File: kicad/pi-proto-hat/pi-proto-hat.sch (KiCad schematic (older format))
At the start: 5 parts, among them P1 Conn_02x20_Odd_Even

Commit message: R1: one GPIO connector, one I2C connector
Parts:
- added J1: Conn_01x24_Male, Connector_PinHeader_2.54mm:PinHeader_1x24_P2.54mm_Vertical, symbol Connector:Conn_01x24_Male
- added J2: Conn_I2C, Connector_PinHeader_2.54mm:PinHeader_1x04_P2.54mm_Vertical, symbol Connector:Conn_01x04_Male
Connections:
- net +3V3: now also J2.4 (Pin_4)
- net GND: now also J2.3 (Pin_3)
- net GPIO10(SPI0_MOSI): now also J1.14 (Pin_14)
- net GPIO11(SPI0_SCK): now also J1.12 (Pin_12)
- net GPIO12(PWM0): now also J1.7 (Pin_7)
- net GPIO13(PWM1): now also J1.6 (Pin_6)
- net GPIO14(TXD0): now also J1.24 (Pin_24)
- net GPIO15(RXD0): now also J1.23 (Pin_23)
- net GPIO16: now also J1.5 (Pin_5)
- net GPIO17(GEN0): now also J1.21 (Pin_21)
- net GPIO18(GEN1)(PWM0): now also J1.20 (Pin_20)
- net GPIO19(SPI1_MISO): now also J1.4 (Pin_4)
- net GPIO2(SDA1): now also J2.2 (Pin_2)
- net GPIO20(SPI1_MOSI): now also J1.3 (Pin_3)
- net GPIO21(SPI1_SCK): now also J1.2 (Pin_2)
- net GPIO22(GEN3): now also J1.18 (Pin_18)
- net GPIO23(GEN4): now also J1.17 (Pin_17)
- net GPIO24(GEN5): now also J1.16 (Pin_16)
- net GPIO25(GEN6): now also J1.15 (Pin_15)
- net GPIO26: now also J1.1 (Pin_1)
- net GPIO27(GEN2): now also J1.19 (Pin_19)
- net GPIO3(SCL1): now also J2.1 (Pin_1)
- net GPIO4(GCLK): now also J1.22 (Pin_22)
- net GPIO5: now also J1.9 (Pin_9)
- net GPIO6: now also J1.8 (Pin_8)
- net GPIO9(SPI0_MISO): now also J1.13 (Pin_13)
- net GPIO7(SPI1_CE_N) renamed GPIO7(SPI1_CE_1)
- net GPIO7(SPI1_CE_1): now also J1.10 (Pin_10)
- net GPIO8(SPI0_CE_N) renamed GPIO8(SPI0_CE_0)
- net GPIO8(SPI0_CE_0): now also J1.11 (Pin_11)
- net ID_SC: no longer names the net of P1.28 (Pin_28)
- net ID_SD: no longer names the net of P1.27 (Pin_27)
- no-connect marks 0 -> 2
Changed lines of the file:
@@
 	1250 2200 2400 2200
 Wire Wire Line
-	2400 2400 1250 2400
-Wire Wire Line
 	1250 2500 2400 2500
 Wire Wire Line
@@
 Wire Wire Line
 	2900 2300 3950 2300
-Wire Wire Line
-	2900 2400 3950 2400
 Wire Wire Line
 	2900 2100 3950 2100
@@
 Text Label 1250 2200 0    50   ~ 0
 GPIO11(SPI0_SCK)
-Text Label 1250 2400 0    50   ~ 0
-ID_SD
 Text Label 1250 2500 0    50   ~ 0
 GPIO5
@@
 Text Label 3950 2600 2    50   ~ 0
 GPIO12(PWM0)
-Text Label 3950 2400 2    50   ~ 0
-ID_SC
 Text Label 3950 2300 2    50   ~ 0
-GPIO7(SPI1_CE_N)
+GPIO7(SPI1_CE_1)
 Text Label 3950 2200 2    50   ~ 0
-GPIO8(SPI0_CE_N)
+GPIO8(SPI0_CE_0)
 Text Label 3950 2100 2    50   ~ 0
 GPIO25(GEN6)
@@
 	3000 1700 3000 2000
 $Comp
-L power:GND #PWR?
+L power:GND #PWR0101
 U 1 1 5E32FD4E
 P 800 1050
-F 0 "#PWR?" H 800 800 50  0001 C CNN
+F 0 "#PWR0101" H 800 800 50  0001 C CNN
 F 1 "GND" H 805 877 50  0000 C CNN
 F 2 "" H 800 1050 50  0001 C CNN
@@
 $EndComp
 $Comp
-L power:+3.3V #PWR?
+L power:+3.3V #PWR0102
 U 1 1 5E330101
 P 800 1700
-F 0 "#PWR?" H 800 1550 50  0001 C CNN
+F 0 "#PWR0102" H 800 1550 50  0001 C CNN
 F 1 "+3.3V" H 815 1873 50  0000 C CNN
 F 2 "" H 800 1700 50  0001 C CNN
@@
 $EndComp
 $Comp
-L power:+5V #PWR?
+L power:+5V #PWR0103
 U 1 1 5E33350C
 P 800 2450
-F 0 "#PWR?" H 800 2300 50  0001 C CNN
+F 0 "#PWR0103" H 800 2300 50  0001 C CNN
 F 1 "+5V" H 815 2623 50  0000 C CNN
 F 2 "" H 800 2450 50  0001 C CNN
@@
 $EndComp
 $Comp
-L power:PWR_FLAG #FLG?
+L power:PWR_FLAG #FLG0101
 U 1 1 5E335D20
 P 800 1500
-F 0 "#FLG?" H 800 1575 50  0001 C CNN
+F 0 "#FLG0101" H 800 1575 50  0001 C CNN
 F 1 "PWR_FLAG" H 800 1673 50  0000 C CNN
 F 2 "" H 800 1500 50  0001 C CNN
@@
 $EndComp
 $Comp
-L power:PWR_FLAG #FLG?
+L power:PWR_FLAG #FLG0102
 U 1 1 5E3368A3
 P 800 2200
-F 0 "#FLG?" H 800 2275 50  0001 C CNN
+F 0 "#FLG0102" H 800 2275 50  0001 C CNN
 F 1 "PWR_FLAG" H 800 2373 50  0000 C CNN
 F 2 "" H 800 2200 50  0001 C CNN
@@
 $EndComp
 $Comp
-L power:PWR_FLAG #FLG?
+L power:PWR_FLAG #FLG0103
 U 1 1 5E337128
 P 800 800
-F 0 "#FLG?" H 800 875 50  0001 C CNN
+F 0 "#FLG0103" H 800 875 50  0001 C CNN
 F 1 "PWR_FLAG" H 800 973 50  0000 C CNN
 F 2 "" H 800 800 50  0001 C CNN
@@
 Wire Wire Line
 	800  2200 800  2450
+$Comp
+L Connector:Conn_01x24_Male J1
+U 1 1 5E33021D
+P 5500 2150
+F 0 "J1" H 5900 700 50  0000 R CNN
+F 1 "Conn_01x24_Male" H 6100 800 50  0000 R CNN
+F 2 "Connector_PinHeader_2.54mm:PinHeader_1x24_P2.54mm_Vertical" H 5500 2150 50  0001 C CNN
+F 3 "~" H 5500 2150 50  0001 C CNN
+	1    5500 2150
+	-1   0    0    1
+$EndComp
+Text Label 4900 950  2    50   ~ 0
+GPIO14(TXD0)
+Text Label 4900 1050 2    50   ~ 0
+GPIO15(RXD0)
+Text Label 4900 1150 2    50   ~ 0
+GPIO4(GCLK)
+Text Label 4900 1250 2    50   ~ 0
+GPIO17(GEN0)
+Text Label 4900 1350 2    50   ~ 0
+GPIO18(GEN1)(PWM0)
+Text Label 4900 1450 2    50   ~ 0
+GPIO27(GEN2)
+Text Label 4900 1550 2    50   ~ 0
+GPIO22(GEN3)
+Text Label 4900 1650 2    50   ~ 0
+GPIO23(GEN4)
+Text Label 4900 1850 2    50   ~ 0
+GPIO25(GEN6)
+Text Label 4900 1950 2    50   ~ 0
+GPIO10(SPI0_MOSI)
+Text Label 4900 2050 2    50   ~ 0
+GPIO9(SPI0_MISO)
+Text Label 4900 2150 2    50   ~ 0
+GPIO11(SPI0_SCK)
+Text Label 4900 2250 2    50   ~ 0
+GPIO8(SPI0_CE_0)
+Text Label 4900 2350 2    50   ~ 0
+GPIO7(SPI1_CE_1)
+Text Label 4900 2450 2    50   ~ 0
+GPIO5
+Text Label 4900 2550 2    50   ~ 0
+GPIO6
+Text Label 4900 2650 2    50   ~ 0
+GPIO12(PWM0)
+Text Label 4900 2750 2    50   ~ 0
+GPIO13(PWM1)
+Text Label 4900 2850 2    50   ~ 0
+GPIO16
+Text Label 4900 2950 2    50   ~ 0
+GPIO19(SPI1_MISO)
+Text Label 4900 3050 2    50   ~ 0
+GPIO20(SPI1_MOSI)
+Text Label 4900 3150 2    50   ~ 0
+GPIO21(SPI1_SCK)
+Text Label 4900 3250 2    50   ~ 0
+GPIO26
+Wire Wire Line
+	4900 950  5300 950
+Wire Wire Line
+	4900 1050 5300 1050
+Wire Wire Line
+	4900 1150 5300 1150
+Wire Wire Line
+	4900 1250 5300 1250
+Wire Wire Line
+	4900 1350 5300 1350
+Wire Wire Line
+	4900 1450 5300 1450
+Wire Wire Line
+	4900 1550 5300 1550
+Wire Wire Line
+	4900 1650 5300 1650
+Wire Wire Line
+	4900 1750 5300 1750
+Wire Wire Line
+	4900 1850 5300 1850
+Wire Wire Line
+	4900 1950 5300 1950
+Wire Wire Line
+	4900 2050 5300 2050
+Wire Wire Line
+	4900 2150 5300 2150
+Wire Wire Line
+	4900 2250 5300 2250
+Wire Wire Line
+	4900 2350 5300 2350
+Wire Wire Line
+	4900 2450 5300 2450
+Wire Wire Line
+	4900 2550 5300 2550
+Wire Wire Line
+	4900 2650 5300 2650
+Wire Wire Line
+	4900 2750 5300 2750
+Wire Wire Line
+	4900 2850 5300 2850
+Wire Wire Line
+	4900 2950 5300 2950
+Wire Wire Line
+	4900 3050 5300 3050
+Wire Wire Line
+	4900 3150 5300 3150
+Wire Wire Line
+	4900 3250 5300 3250
+Text Label 4900 1750 2    50   ~ 0
+GPIO24(GEN5)
+NoConn ~ 2400 2400
+NoConn ~ 2900 2400
+$Comp
+L Connector:Conn_01x04_Male J2
+U 1 1 5E3AE486
+P 6400 1150
+F 0 "J2" H 6550 700 50  0000 R CNN
+F 1 "Conn_I2C" H 6650 800 50  0000 R CNN
+F 2 "Connector_PinHeader_2.54mm:PinHeader_1x04_P2.54mm_Vertical" H 6400 1150 50  0001 C CNN
+F 3 "~" H 6400 1150 50  0001 C CNN
+	1    6400 1150
+	-1   0    0    1
+$EndComp
+$Comp
+L power:+3.3V #PWR0104
+U 1 1 5E3B69CB
+P 6050 950
+F 0 "#PWR0104" H 6050 800 50  0001 C CNN
+F 1 "+3.3V" V 6050 1200 50  0000 C CNN
+F 2 "" H 6050 950 50  0000 C CNN
+F 3 "" H 6050 950 50  0000 C CNN
+	1    6050 950
+	0    -1   -1   0
+$EndComp
+$Comp
+L power:GND #PWR0105
+U 1 1 5E3BF524
+P 6050 1050
+F 0 "#PWR0105" H 6050 800 50  0001 C CNN
+F 1 "GND" H 6050 900 50  0000 C CNN
+F 2 "" H 6050 1050 50  0000 C CNN
+F 3 "" H 6050 1050 50  0000 C CNN
+	1    6050 1050
+	0    1    1    0
+$EndComp
+Text Label 6050 1250 2    50   ~ 0
+GPIO3(SCL1)
+Text Label 6050 1150 2    50   ~ 0
+GPIO2(SDA1)
+Wire Wire Line
+	6050 950  6200 950
+Wire Wire Line
+	6050 1050 6200 1050
+Wire Wire Line
+	6050 1150 6200 1150
+Wire Wire Line
+	6050 1250 6200 1250
 $EndSCHEMATC

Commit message: R2: 1xUART+GND, 2xI2C+VCC+GND
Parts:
- added I2C2: Conn_I2C, Connector_PinHeader_2.54mm:PinHeader_1x04_P2.54mm_Vertical, symbol Connector:Conn_01x04_Male
- added UART1: Conn_01x03_Male, Connector_PinHeader_2.54mm:PinHeader_1x03_P2.54mm_Vertical, symbol Connector:Conn_01x03_Male
- J1: value Conn_01x24_Male -> Conn_01x22_Male; footprint Connector_PinHeader_2.54mm:PinHeader_1x24_P2.54mm_Vertical -> Connector_PinHeader_2.54mm:PinHeader_1x22_P2.54mm_Vertical; symbol Connector:Conn_01x24_Male -> Connector:Conn_01x22_Male
- renumbered J2 to I2C1
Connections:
- net +3V3: now also I2C2.4 (Pin_4)
- net GND: now also I2C2.3 (Pin_3), UART1.1 (Pin_1)
- net GPIO14(TXD0): now also UART1.3 (Pin_3); no longer J1.24 (Pin_24)
- net GPIO15(RXD0): now also UART1.2 (Pin_2); no longer J1.23 (Pin_23)
- net GPIO17(GEN0): now also J1.20 (Pin_20); no longer J1.21 (Pin_21)
- net GPIO18(GEN1)(PWM0): now also J1.21 (Pin_21); no longer J1.20 (Pin_20)
- net GPIO2(SDA1): now also I2C1.1 (Pin_1), I2C2.1 (Pin_1); no longer I2C1.2 (Pin_2)
- net GPIO22(GEN3): now also J1.17 (Pin_17); no longer J1.18 (Pin_18)
- net GPIO23(GEN4): now also J1.18 (Pin_18); no longer J1.17 (Pin_17)
- net GPIO3(SCL1): now also I2C1.2 (Pin_2), I2C2.2 (Pin_2); no longer I2C1.1 (Pin_1)
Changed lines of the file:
@@
 Sheet 1 1
 Title "Pi-Proto-Hat"
-Date "2020-01-30"
-Rev "1"
+Date "2020-02-15"
+Rev "2"
 Comp "Bernhard Bablok"
 Comment1 "https://github.com/bablokb/pi-proto-hat"
@@
 	800  2200 800  2450
 $Comp
-L Connector:Conn_01x24_Male J1
+L Connector:Conn_01x22_Male J1
 U 1 1 5E33021D
-P 5500 2150
+P 5500 2050
 F 0 "J1" H 5900 700 50  0000 R CNN
-F 1 "Conn_01x24_Male" H 6100 800 50  0000 R CNN
-F 2 "Connector_PinHeader_2.54mm:PinHeader_1x24_P2.54mm_Vertical" H 5500 2150 50  0001 C CNN
-F 3 "~" H 5500 2150 50  0001 C CNN
-	1    5500 2150
+F 1 "Conn_01x22_Male" H 6150 800 50  0000 R CNN
+F 2 "Connector_PinHeader_2.54mm:PinHeader_1x22_P2.54mm_Vertical" H 5500 2050 50  0001 C CNN
+F 3 "~" H 5500 2050 50  0001 C CNN
+	1    5500 2050
 	-1   0    0    1
 $EndComp
 Text Label 4900 950  2    50   ~ 0
-GPIO14(TXD0)
+GPIO4(GCLK)
+Text Label 4900 1150 2    50   ~ 0
+GPIO17(GEN0)
 Text Label 4900 1050 2    50   ~ 0
-GPIO15(RXD0)
-Text Label 4900 1150 2    50   ~ 0
-GPIO4(GCLK)
+GPIO18(GEN1)(PWM0)
 Text Label 4900 1250 2    50   ~ 0
-GPIO17(GEN0)
-Text Label 4900 1350 2    50   ~ 0
-GPIO18(GEN1)(PWM0)
+GPIO27(GEN2)
 Text Label 4900 1450 2    50   ~ 0
-GPIO27(GEN2)
-Text Label 4900 1550 2    50   ~ 0
 GPIO22(GEN3)
 Text Label 4900 1650 2    50   ~ 0
-GPIO23(GEN4)
+GPIO25(GEN6)
+Text Label 4900 1750 2    50   ~ 0
+GPIO10(SPI0_MOSI)
 Text Label 4900 1850 2    50   ~ 0
-GPIO25(GEN6)
+GPIO9(SPI0_MISO)
 Text Label 4900 1950 2    50   ~ 0
-GPIO10(SPI0_MOSI)
+GPIO11(SPI0_SCK)
 Text Label 4900 2050 2    50   ~ 0
-GPIO9(SPI0_MISO)
+GPIO8(SPI0_CE_0)
 Text Label 4900 2150 2    50   ~ 0
-GPIO11(SPI0_SCK)
+GPIO7(SPI1_CE_1)
 Text Label 4900 2250 2    50   ~ 0
-GPIO8(SPI0_CE_0)
+GPIO5
 Text Label 4900 2350 2    50   ~ 0
-GPIO7(SPI1_CE_1)
+GPIO6
 Text Label 4900 2450 2    50   ~ 0
-GPIO5
+GPIO12(PWM0)
 Text Label 4900 2550 2    50   ~ 0
-GPIO6
+GPIO13(PWM1)
 Text Label 4900 2650 2    50   ~ 0
-GPIO12(PWM0)
+GPIO16
 Text Label 4900 2750 2    50   ~ 0
-GPIO13(PWM1)
+GPIO19(SPI1_MISO)
 Text Label 4900 2850 2    50   ~ 0
-GPIO16
+GPIO20(SPI1_MOSI)
 Text Label 4900 2950 2    50   ~ 0
-GPIO19(SPI1_MISO)
+GPIO21(SPI1_SCK)
 Text Label 4900 3050 2    50   ~ 0
-GPIO20(SPI1_MOSI)
-Text Label 4900 3150 2    50   ~ 0
-GPIO21(SPI1_SCK)
-Text Label 4900 3250 2    50   ~ 0
 GPIO26
 Wire Wire Line
@@
 Wire Wire Line
 	4900 3050 5300 3050
-Wire Wire Line
-	4900 3150 5300 3150
-Wire Wire Line
-	4900 3250 5300 3250
-Text Label 4900 1750 2    50   ~ 0
+Text Label 4900 1550 2    50   ~ 0
 GPIO24(GEN5)
 NoConn ~ 2400 2400
 NoConn ~ 2900 2400
 $Comp
-L Connector:Conn_01x04_Male J2
+L Connector:Conn_01x04_Male I2C1
 U 1 1 5E3AE486
 P 6400 1150
-F 0 "J2" H 6550 700 50  0000 R CNN
-F 1 "Conn_I2C" H 6650 800 50  0000 R CNN
+F 0 "I2C1" H 6750 700 50  0000 R CNN
+F 1 "Conn_I2C" H 6800 800 50  0000 R CNN
 F 2 "Connector_PinHeader_2.54mm:PinHeader_1x04_P2.54mm_Vertical" H 6400 1150 50  0001 C CNN
 F 3 "~" H 6400 1150 50  0001 C CNN
@@
 	0    1    1    0
 $EndComp
+Text Label 6050 1150 2    50   ~ 0
+GPIO3(SCL1)
 Text Label 6050 1250 2    50   ~ 0
+GPIO2(SDA1)
+Wire Wire Line
+	6050 950  6200 950
+Wire Wire Line
+	6050 1050 6200 1050
+Wire Wire Line
+	6050 1150 6200 1150
+Wire Wire Line
+	6050 1250 6200 1250
+$Comp
+L Connector:Conn_01x04_Male I2C2
+U 1 1 5E46D17D
+P 7300 1150
+F 0 "I2C2" H 7600 700 50  0000 R CNN
+F 1 "Conn_I2C" H 7650 800 50  0000 R CNN
+F 2 "Connector_PinHeader_2.54mm:PinHeader_1x04_P2.54mm_Vertical" H 7300 1150 50  0001 C CNN
+F 3 "~" H 7300 1150 50  0001 C CNN
+	1    7300 1150
+	-1   0    0    1
+$EndComp
+$Comp
+L power:+3.3V #PWR0106
+U 1 1 5E46D187
+P 6950 950
+F 0 "#PWR0106" H 6950 800 50  0001 C CNN
+F 1 "+3.3V" V 6950 1200 50  0000 C CNN
+F 2 "" H 6950 950 50  0000 C CNN
+F 3 "" H 6950 950 50  0000 C CNN
+	1    6950 950
+	0    -1   -1   0
+$EndComp
+$Comp
+L power:GND #PWR0107
+U 1 1 5E46D191
+P 6950 1050
+F 0 "#PWR0107" H 6950 800 50  0001 C CNN
+F 1 "GND" H 6950 900 50  0000 C CNN
+F 2 "" H 6950 1050 50  0000 C CNN
+F 3 "" H 6950 1050 50  0000 C CNN
+	1    6950 1050
+	0    1    1    0
+$EndComp
+Text Label 6950 1150 2    50   ~ 0
 GPIO3(SCL1)
-Text Label 6050 1150 2    50   ~ 0
+Text Label 6950 1250 2    50   ~ 0
 GPIO2(SDA1)
 Wire Wire Line
-	6050 950  6200 950
-Wire Wire Line
-	6050 1050 6200 1050
-Wire Wire Line
-	6050 1150 6200 1150
-Wire Wire Line
-	6050 1250 6200 1250
+	6950 950  7100 950
+Wire Wire Line
+	6950 1050 7100 1050
+Wire Wire Line
+	6950 1150 7100 1150
+Wire Wire Line
+	6950 1250 7100 1250
+$Comp
+L Connector:Conn_01x03_Male UART1
+U 1 1 5E470F02
+P 8100 1100
+F 0 "UART1" H 8500 700 50  0000 R CNN
+F 1 "Conn_01x03_Male" H 8600 800 50  0000 R CNN
+F 2 "Connector_PinHeader_2.54mm:PinHeader_1x03_P2.54mm_Vertical" H 8100 1100 50  0001 C CNN
+F 3 "~" H 8100 1100 50  0001 C CNN
+	1    8100 1100
+	-1   0    0    1
+$EndComp
+Text Label 7900 1000 2    50   ~ 0
+GPIO14(TXD0)
+Text Label 7900 1100 2    50   ~ 0
+GPIO15(RXD0)
+$Comp
+L power:GND #PWR0108
+U 1 1 5E4850A5
+P 7900 1200
+F 0 "#PWR0108" H 7900 950 50  0001 C CNN
+F 1 "GND" H 7900 1050 50  0000 C CNN
+F 2 "" H 7900 1200 50  0000 C CNN
+F 3 "" H 7900 1200 50  0000 C CNN
+	1    7900 1200
+	0    1    1    0
+$EndComp
+Text Label 4900 1350 2    50   ~ 0
+GPIO23(GEN4)
 $EndSCHEMATC

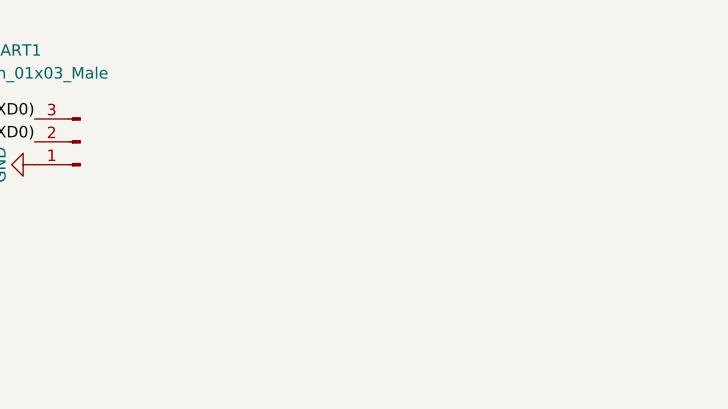
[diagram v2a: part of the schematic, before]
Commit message: R3: VCC+GND connector 22x02
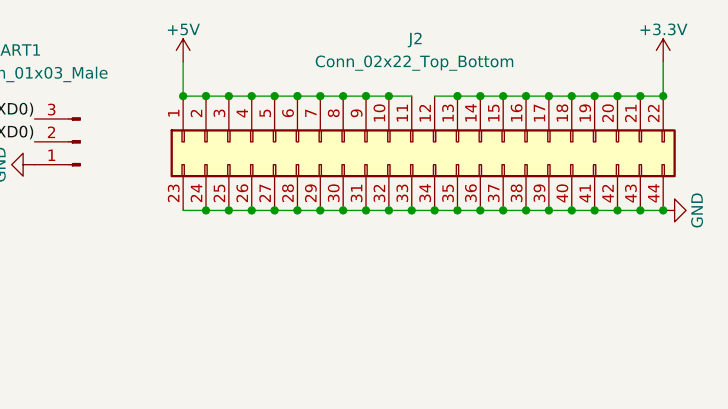
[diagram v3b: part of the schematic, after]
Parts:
- added J2: Conn_02x22_Top_Bottom, Proto_Area:Proto_Area_22x02, symbol Connector_Generic:Conn_02x22_Top_Bottom
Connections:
- net +3V3: now also J2.12 (Pin_12), J2.13 (Pin_13), J2.14 (Pin_14), J2.15 (Pin_15), J2.16 (Pin_16), J2.17 (Pin_17), J2.18 (Pin_18), J2.19 (Pin_19), J2.20 (Pin_20), J2.21 (Pin_21), J2.22 (Pin_22)
- net +5V: now also J2.1 (Pin_1), J2.10 (Pin_10), J2.11 (Pin_11), J2.2 (Pin_2), J2.3 (Pin_3), J2.4 (Pin_4), J2.5 (Pin_5), J2.6 (Pin_6), J2.7 (Pin_7), J2.8 (Pin_8), J2.9 (Pin_9)
- net GND: now also J2.23 (Pin_23), J2.24 (Pin_24), J2.25 (Pin_25), J2.26 (Pin_26), J2.27 (Pin_27), J2.28 (Pin_28), J2.29 (Pin_29), J2.30 (Pin_30), J2.31 (Pin_31), J2.32 (Pin_32), J2.33 (Pin_33), J2.34 (Pin_34), J2.35 (Pin_35), J2.36 (Pin_36), J2.37 (Pin_37), J2.38 (Pin_38), J2.39 (Pin_39), J2.40 (Pin_40), J2.41 (Pin_41), J2.42 (Pin_42), J2.43 (Pin_43), J2.44 (Pin_44)
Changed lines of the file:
@@
 Title "Pi-Proto-Hat"
 Date "2020-02-15"
-Rev "2"
+Rev "3"
 Comp "Bernhard Bablok"
 Comment1 "https://github.com/bablokb/pi-proto-hat"
@@
 	4900 2250 5300 2250
 Wire Wire Line
-	4900 2350 5300 2350
-Wire Wire Line
-	4900 2450 5300 2450
-Wire Wire Line
 	4900 2550 5300 2550
 Wire Wire Line
@@
 Wire Wire Line
 	4900 2750 5300 2750
-Wire Wire Line
-	4900 2850 5300 2850
-Wire Wire Line
-	4900 2950 5300 2950
 Wire Wire Line
 	4900 3050 5300 3050
@@
 Text Label 4900 1350 2    50   ~ 0
 GPIO23(GEN4)
+$Comp
+L Connector_Generic:Conn_02x22_Top_Bottom J2
+U 1 1 5E47EDE2
+P 9550 1100
+F 0 "J2" V 9100 1050 50  0000 L CNN
+F 1 "Conn_02x22_Top_Bottom" V 9200 650 50  0000 L CNN
+F 2 "Proto_Area:Proto_Area_22x02" H 9550 1100 50  0001 C CNN
+F 3 "~" H 9550 1100 50  0001 C CNN
+	1    9550 1100
+	0    -1   1    0
+$EndComp
+Wire Wire Line
+	4900 2350 5300 2350
+Wire Wire Line
+	4900 2850 5300 2850
+Wire Wire Line
+	8550 1400 8650 1400
+Connection ~ 8650 1400
+Wire Wire Line
+	8650 1400 8750 1400
+Connection ~ 8750 1400
+Wire Wire Line
+	8750 1400 8850 1400
+Connection ~ 8850 1400
+Wire Wire Line
+	8850 1400 8950 1400
+Connection ~ 8950 1400
+Wire Wire Line
+	8950 1400 9050 1400
+Connection ~ 9050 1400
+Wire Wire Line
+	9050 1400 9150 1400
+Connection ~ 9150 1400
+Wire Wire Line
+	9150 1400 9250 1400
+Connection ~ 9250 1400
+Wire Wire Line
+	9250 1400 9350 1400
+Connection ~ 9350 1400
+Wire Wire Line
+	9350 1400 9450 1400
+Connection ~ 9450 1400
+Wire Wire Line
+	9450 1400 9550 1400
+Connection ~ 9550 1400
+Wire Wire Line
+	9550 1400 9650 1400
+Connection ~ 9650 1400
+Wire Wire Line
+	9650 1400 9750 1400
+Connection ~ 9750 1400
+Wire Wire Line
+	9750 1400 9850 1400
+Connection ~ 9850 1400
+Wire Wire Line
+	9850 1400 9950 1400
+Connection ~ 9950 1400
+Wire Wire Line
+	9950 1400 10050 1400
+Connection ~ 10050 1400
+Wire Wire Line
+	10050 1400 10150 1400
+Connection ~ 10150 1400
+Wire Wire Line
+	10150 1400 10250 1400
+Connection ~ 10250 1400
+Wire Wire Line
+	10250 1400 10350 1400
+Connection ~ 10350 1400
+Wire Wire Line
+	10350 1400 10450 1400
+Connection ~ 10450 1400
+Wire Wire Line
+	10450 1400 10550 1400
+Connection ~ 10550 1400
+Wire Wire Line
+	10550 1400 10650 1400
+$Comp
+L power:GND #PWR0109
+U 1 1 5E49E1AA
+P 10650 1400
+F 0 "#PWR0109" H 10650 1150 50  0001 C CNN
+F 1 "GND" H 10650 1250 50  0000 C CNN
+F 2 "" H 10650 1400 50  0000 C CNN
+F 3 "" H 10650 1400 50  0000 C CNN
+	1    10650 1400
+	0    -1   -1   0
+$EndComp
+Connection ~ 10650 1400
+$Comp
+L power:+5V #PWR0110
+U 1 1 5E4A9750
+P 8550 750
+F 0 "#PWR0110" H 8550 600 50  0001 C CNN
+F 1 "+5V" H 8550 890 50  0000 C CNN
+F 2 "" H 8550 750 50  0000 C CNN
+F 3 "" H 8550 750 50  0000 C CNN
+	1    8550 750
+	1    0    0    -1
+$EndComp
+$Comp
+L power:+3.3V #PWR0111
+U 1 1 5E4AA778
+P 10650 750
+F 0 "#PWR0111" H 10650 600 50  0001 C CNN
+F 1 "+3.3V" H 10650 890 50  0000 C CNN
+F 2 "" H 10650 750 50  0000 C CNN
+F 3 "" H 10650 750 50  0000 C CNN
+	1    10650 750
+	1    0    0    -1
+$EndComp
+Wire Wire Line
+	8550 900  8650 900
+Connection ~ 8650 900
+Wire Wire Line
+	8650 900  8750 900
+Connection ~ 8750 900
+Wire Wire Line
+	8750 900  8850 900
+Connection ~ 8850 900
+Wire Wire Line
+	8850 900  8950 900
+Connection ~ 8950 900
+Wire Wire Line
+	8950 900  9050 900
+Connection ~ 9050 900
+Wire Wire Line
+	9050 900  9150 900
+Connection ~ 9150 900
+Wire Wire Line
+	9150 900  9250 900
+Connection ~ 9250 900
+Wire Wire Line
+	9250 900  9350 900
+Connection ~ 9350 900
+Wire Wire Line
+	9350 900  9450 900
+Connection ~ 9450 900
+Wire Wire Line
+	9450 900  9550 900
+Wire Wire Line
+	9650 900  9750 900
+Connection ~ 9750 900
+Wire Wire Line
+	9750 900  9850 900
+Connection ~ 9850 900
+Wire Wire Line
+	9850 900  9950 900
+Connection ~ 9950 900
+Wire Wire Line
+	9950 900  10050 900
+Connection ~ 10050 900
+Wire Wire Line
+	10050 900  10150 900
+Connection ~ 10150 900
+Wire Wire Line
+	10150 900  10250 900
+Connection ~ 10250 900
+Wire Wire Line
+	10250 900  10350 900
+Connection ~ 10350 900
+Wire Wire Line
+	10350 900  10450 900
+Connection ~ 10450 900
+Wire Wire Line
+	10450 900  10550 900
+Connection ~ 10550 900
+Wire Wire Line
+	10550 900  10650 900
+Wire Wire Line
+	10650 750  10650 900
+Connection ~ 10650 900
+Wire Wire Line
+	8550 750  8550 900
+Connection ~ 8550 900
+Wire Wire Line
+	4900 2450 5300 2450
+Wire Wire Line
+	4900 2950 5300 2950
 $EndSCHEMATC
